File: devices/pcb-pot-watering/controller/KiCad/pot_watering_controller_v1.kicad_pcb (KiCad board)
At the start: 2 copper layers, 64.6 x 87.1 mm, 42 parts, among them SW1 SW_Push, SW2 SW_Push, U1 ESP32-WROOM-32, U2 LPS33HWTR, U3 LPS33HWTR, U4 MCZ33996EK, U5 LIS3DH, U7 XC6206PxxxMR

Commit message: Add IC controller
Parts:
- removed U7: XC6206PxxxMR, Package_TO_SOT_SMD:SOT-223
- added C5: 100nF, Capacitor_SMD:C_0805_2012Metric, B.Cu at (111.9, 139.1)
- added U6: AMS1117-3.3, Package_TO_SOT_SMD:SOT-223-3_TabPin2, B.Cu at (125.3, 147.9)
- moved C4 3.41 mm to (111.9, 142.5)
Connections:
- U4 pad 6: +3V3 -> VCC
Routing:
- net VCC: track 265.3 -> 280.9 mm, vias 5 -> 6
- net +3V3: track 290.5 -> 293.6 mm, vias 27 -> 26
- net GND: track 497.5 -> 499.6 mm
- net EP: track 0.97 -> 0.00 mm
- net NS_sensor_07: track 70.5 -> 71.4 mm
- net NS_pumpes: track 37.7 -> 38.5 mm
- added copper zone on B.Cu, net +3V3
- added copper zone on B.Cu, net EP
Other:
- board text added: "Watering Pot Automation V1.4 - 21.09.2020"
- board text removed: "Watering Pot Automation V1.3 - 10.09.2020"

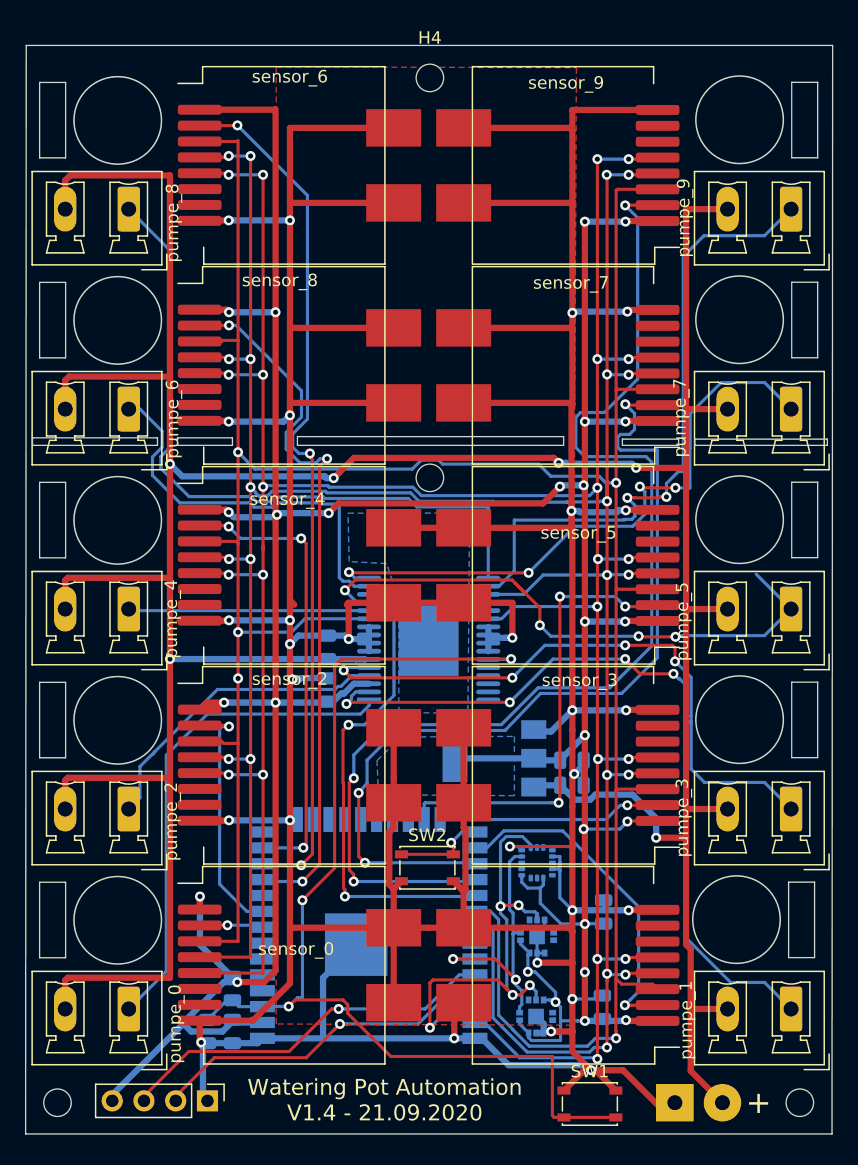
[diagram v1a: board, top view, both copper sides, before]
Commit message: all sensors actor working
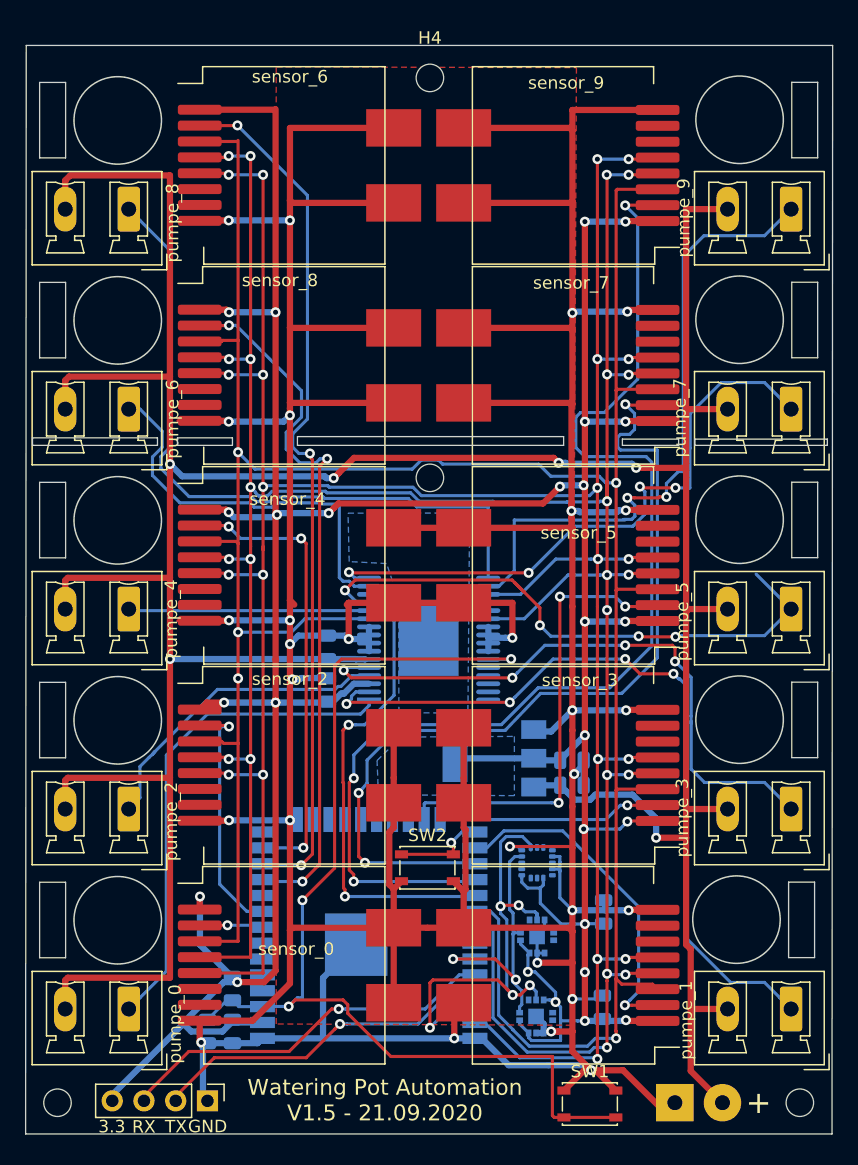
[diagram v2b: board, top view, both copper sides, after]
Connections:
- U4 pad 19: MISO -> MOSI
- U4 pad 22: MOSI -> MISO
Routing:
- net MOSI: track 233.7 -> 234.5 mm, vias 22 -> 21
- net MISO: track 235.4 -> 236.2 mm, vias 21 -> 22
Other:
- board text added: "*"
- board text added: "3.3"
- board text added: "GND"
- board text added: "RX"
- board text added: "TX"
- board text added: "Watering Pot Automation V1.5 - 21.09.2020"
- board text removed: "Watering Pot Automation V1.4 - 21.09.2020"
